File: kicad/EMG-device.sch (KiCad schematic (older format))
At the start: 53 parts

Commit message: schematics done
schematics 1.0 done
BOM updated, but not ready
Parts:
- removed C? (x2): 0.1uF, symbol C_Small
- removed R? (x3): R_Small, symbol R_Small
- added C? (x3): 47uF, symbol CP
- added R? (x2): 1M, symbol R_Small
- added R? (x2): 10k, symbol R_Small
- added TP? (x13): TEST, symbol TEST
- added U?: MAX1720, symbol MAX1720
- C?: value 0.01uF -> 220pF
- C?: value 1uF -> 80pF
- R?: value Rg -> 470
- R?: value R_Small -> 10k
- R?: value R_Small -> 150K
- R? (x2): value R_Small -> 150k
- R?: value 10M -> 100k
- R?: value R_Small -> 80k
- R?: value R? -> 80k
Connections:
- net ADC: now also R?.1, TP?.1
- net GND: now also U?.3 (+), C?.1, C?.2, R?.2, R?.2, R?.2, U?.4 (GND); no longer U?.10 (+), U?.12 (+)
- net Input1: now also R?.1
- net Input2: now also R?.1
- net V-: now also C?.2, U?.1 (Vout)
- net at U?.12 ((PCINT22/OC0A/AIN0)PD6): now also TP?.1
- net at U?.16 ((PCINT2/OC1B/~SS~)PB2): now also TP?.1
- net at U?.17 ((PCINT3/OC2A/MOSI)PB3): now also TP?.1
- net at U?.18 ((PCINT4/MISO)PB4): now also TP?.1
- net at U?.19 ((PCINT5/SCK)PB5): now also TP?.1
- net at U?.24 ((PCINT9/ADC1)PC1): now also TP?.1
- net at U?.6: now also R?.2, TP?.1; no longer R?.2
- net at C?.2, U?.1: now also C?.1, R?.1, TP?.1; no longer R?.1
- net at R?.1, R?.2: now also U?.2 (-); no longer U?.2 (-)
- net at R?.1, U?.7: now also R?.2, TP?.1
- net at C?.1, D?.A, D?.C: now also U?.7, TP?.1; no longer U?.1
- net at C?.2, D?.A, R?.1: now also U?.6 (-); no longer U?.2 (-)
- net at R?.2: now also R?.1, U?.1, U?.5 (+), TP?.1; no longer U?.3 (+)
- net at D?.C, R?.1: now also U?.10 (+); no longer U?.5 (+)
- net at R?.1, R?.2: now also U?.9 (-); no longer U?.6 (-)
- net at C?.2, R?.1, R?.2: now also U?.2 (-); no longer U?.9 (-)
- net at U?.13 (-): now also R?.1, R?.2
- new net: R?.2, TP?.1, U?.12 (+), U?.8
- new net: C?.2, U?.3 (C-)
- new net: C?.1, U?.6 (C+)
- new net 5V: C?.1, U?.2 (Vin), U?.5 (SHDN)
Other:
- note added: "G (variable pos)= 1 + R2/R1\n"
- note added: "G=-1"
- note added: "G=-15"
- note added: "G=-1\n"
- note added: "G=-R2/R1"
- note added: "G=1"
- note added: "G=1+50k/Rg\nINA121"
- note added: "G=100"
- note added: "Input current bias \nreturn path"
- note added: "Input current bias resistor formula"
- note added: "Negative voltage rail generator"
- note added: "Rb = R1/R2"
- note added: "fc = 1/sqrt(2*pi*R*C)"
- note added: "fc = 160Hz"
- note added: "fc = 70Hz"
- note added: "other possibility is inst op amp. + op amp + rectification + high passs + low pass"
- note added: "terminating resistor,\ncheck if needed\n"
- note added: "variable op amp\n"
- note removed: "ADD RESISTORS TO THE OP AMP INPUTS\nCalculate values for filters\n\n"
- note removed: "as high as possible\n"
- note removed: "calculate the value\n"
- note removed: "variable inverter\n"
- moved on the sheet: C?, D?, R?, U?A, U?B, U?C, U?D

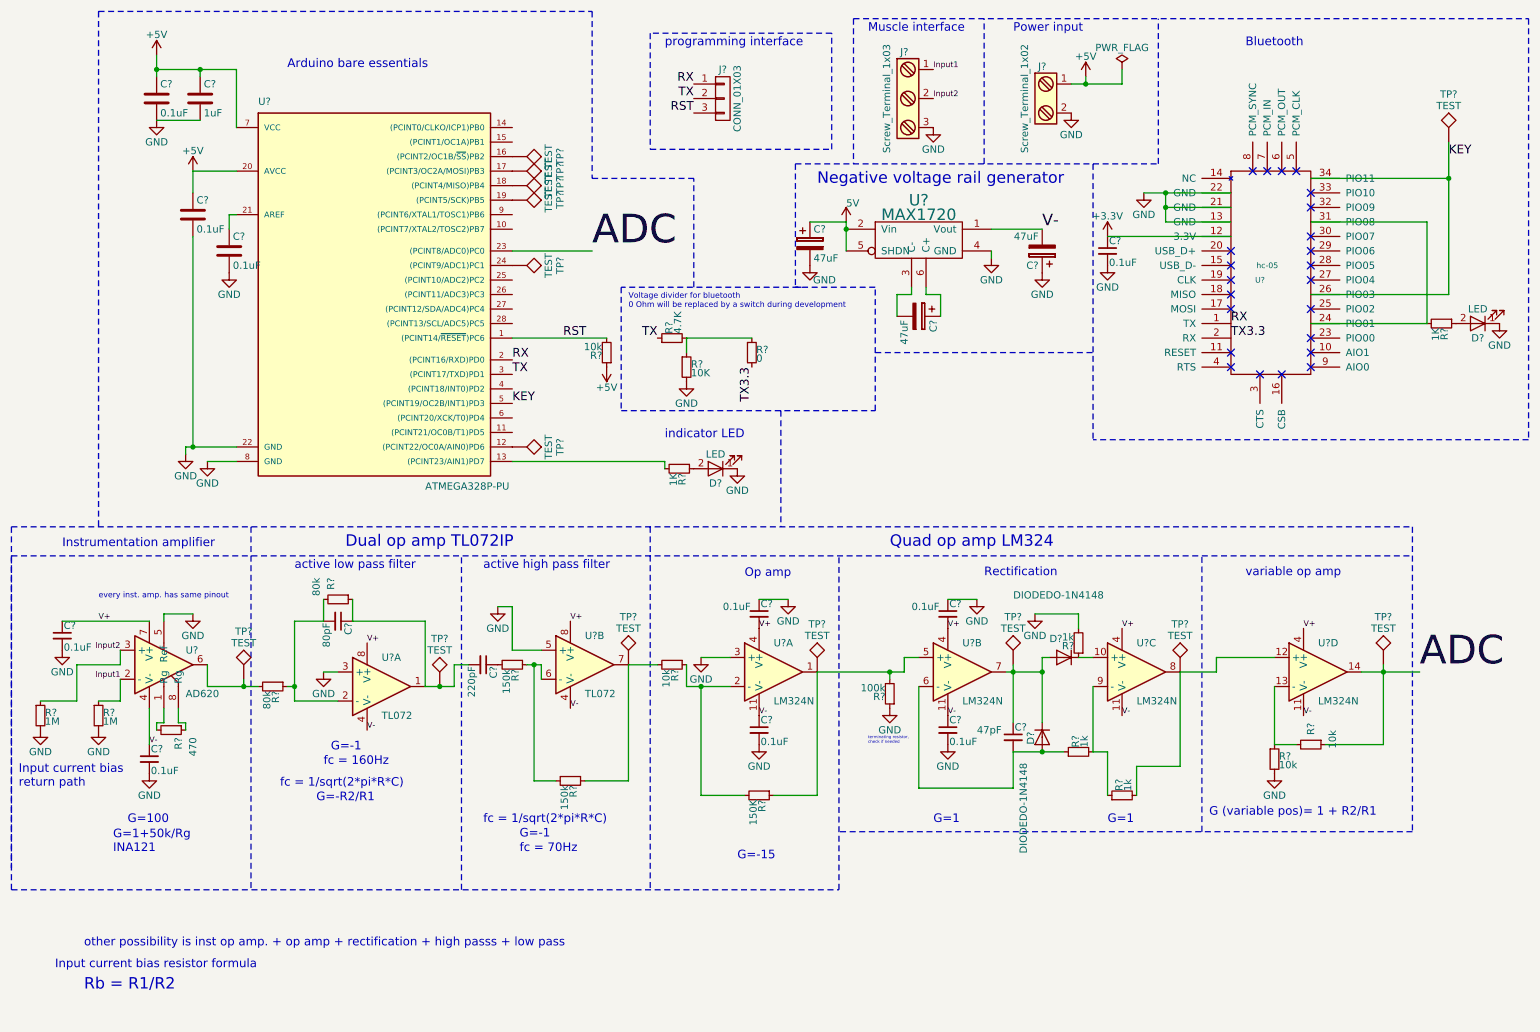
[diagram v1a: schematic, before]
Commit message: BOM done, added missing components to schematics, added footpints
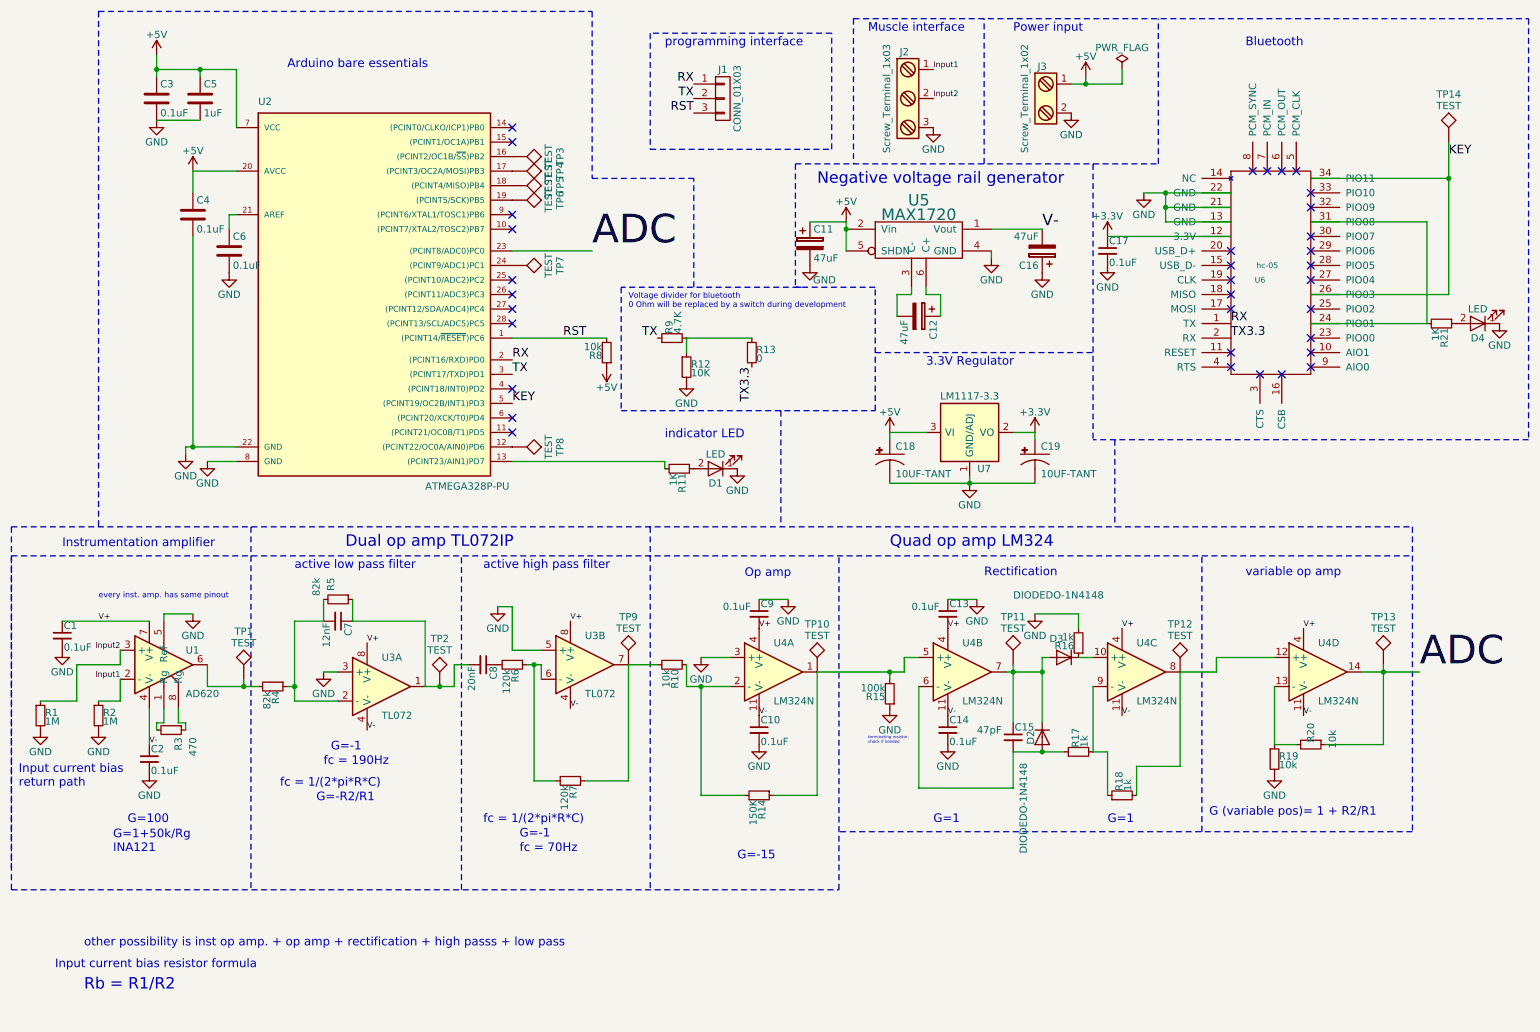
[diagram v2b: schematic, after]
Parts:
- added C18, C19: 10UF-TANT, Capacitors_SMD:C_1206_HandSoldering, symbol 10UF-TANT
- added U7: LM1117-3.3, TO_SOT_Packages_SMD:TO-252-3_TabPin2, symbol LM1117-3.3
- C1, C10, C13, C14, C17, C2, C3, C4, C6, C9: renamed from C?; footprint (none) -> Capacitors_SMD:C_1206_HandSoldering
- C11, C12, C16: renamed from C?; footprint (none) -> Capacitors_SMD:CP_Elec_5x5.3
- C15, C5: renamed from C?; footprint (none) -> Capacitors_SMD:C_0603_HandSoldering
- C7: renamed from C?; value 80pF -> 12nF; footprint (none) -> Capacitors_SMD:C_0603_HandSoldering
- C8: renamed from C?; value 220pF -> 20nF; footprint (none) -> Capacitors_SMD:C_0603_HandSoldering
- D1, D4: renamed from D?; footprint (none) -> LEDs:LED_0603_HandSoldering
- D2, D3: renamed from D?; footprint DO-1N4148 -> adafruit:SOD-123
- J1: renamed from J?; footprint (none) -> Pin_Headers:Pin_Header_Straight_1x03_Pitch2.54mm
- J2: renamed from J?; footprint (none) -> Connectors_Terminal_Blocks:TerminalBlock_Altech_AK300-3_P5.00mm
- J3: renamed from J?; footprint (none) -> Connectors_Terminal_Blocks:TerminalBlock_Altech_AK300-2_P5.00mm
- R1, R10, R11, R12, R13, R14, R15, R16, R17, R18, R19, R2, R20, R21, R3, R8, R9: renamed from R?; footprint (none) -> Resistors_SMD:R_0603_HandSoldering
- R4, R5: renamed from R?; value 80k -> 82k; footprint (none) -> Resistors_SMD:R_0603_HandSoldering
- R6, R7: renamed from R?; value 150k -> 120k; footprint (none) -> Resistors_SMD:R_0603_HandSoldering
- TP1, TP10, TP11, TP12, TP13, TP14, TP2, TP3, TP4, TP5, TP6, TP7, TP8, TP9: renamed from TP?; footprint (none) -> Measurement_Points:Measurement_Point_Round-SMD-Pad_Big
- U1, U3: renamed from U?; footprint (none) -> Housings_DIP:DIP-8_W7.62mm_Socket
- U2: renamed from U?; footprint DIL28 -> Housings_DIP:DIP-28_W7.62mm_Socket
- U4: renamed from U?; footprint (none) -> Housings_DIP:DIP-14_W7.62mm_Socket
- U5: renamed from U?; footprint (none) -> Housings_SSOP:TSOP-6_1.65x3.05mm_Pitch0.95mm
- U6: renamed from U?; footprint (none) -> Bluetooth:HC-05
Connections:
- net 5V is gone; now on net +5V: C11.1, U5.2 (Vin), U5.5 (SHDN)
- net +3V3: now also C19.A (+), U7.2 (VO), U7.4 (VO)
- net +5V: now also C18.A (+), U7.3 (VI)
- net GND: now also C18.C (-), C19.C (-), U7.1 (GND/ADJ)
- no-connect marks 23 -> 34
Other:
- note added: "3.3V Regulator"
- note added: "fc = 1/(2*pi*R*C)"
- note added: "fc = 190Hz"
- note removed: "fc = 1/sqrt(2*pi*R*C)"
- note removed: "fc = 160Hz"

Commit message: layout done, some changes in schematics
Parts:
- removed C18, C19: 10UF-TANT, Capacitors_SMD:C_1206_HandSoldering, symbol 10UF-TANT
- added C18, C19: 10uF, Capacitors_Tantalum_SMD:CP_Tantalum_Case-U_EIA-6032-15_Hand, symbol CP
- added JP1, JP2, JP3, JP4: Jumper, Wire_Connections_Bridges:WireConnection_2.00mmDrill, symbol Jumper
- added JP5: Jumper, Wire_Pads:SolderWirePad_2x_1mmDrill, symbol Jumper
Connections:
- net V+ is gone; now on net +5V: C1.1, C13.2, C9.2, U1.7 (V+), U3.8 (V+), U3.8 (V+), U4.4 (V+), U4.4 (V+), U4.4 (V+), U4.4 (V+)
- net +3V3: now also C19.1
- net +5V: now also C18.1
- net GND: now also C18.2, C19.2, JP1.1, JP1.2, JP2.1, JP2.2, JP3.1, JP3.2, JP4.1, JP4.2, JP5.1, JP5.2
- net KEY: no longer U2.5 ((PCINT19/OC2B/INT1)PD3)
- net RX: now also J1.2 (P2), U2.4 ((PCINT18/INT0)PD2); no longer J1.1 (P1)
- net TX: now also J1.1 (P1); no longer J1.2 (P2)
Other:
- moved on the sheet: C13, C14
